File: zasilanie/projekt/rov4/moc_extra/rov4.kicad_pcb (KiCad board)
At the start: 2 copper layers, 124.5 x 68.6 mm, 18 parts, among them J43 Torpedy_serwo_7v, J44 Extra, J45 Extra, J46 Manip_serwo, J47 Extra, J48 Extra, J53 HP_IN, J60 HP_OUT, U4 lm2596, U5 lm2596

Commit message: sprzątanie
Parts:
- removed the REF** at (152.3, 101.8)
- removed the REF** at (152.3, 48.6)
- removed the REF** at (43.0, 102.0)
- removed the REF** at (43.0, 48.6)
- added REF**: MountingHole_3.2mm_M3_Pad, MountingHole:MountingHole_3.2mm_M3_Pad, F.Cu at (154.0, 29.1)
- added REF**: MountingHole_3.2mm_M3_Pad, MountingHole:MountingHole_3.2mm_M3_Pad, F.Cu at (154.0, 87.5)
- added REF**: MountingHole_3.2mm_M3_Pad, MountingHole:MountingHole_3.2mm_M3_Pad, F.Cu at (39.7, 87.5)
- added REF**: MountingHole_3.2mm_M3_Pad, MountingHole:MountingHole_3.2mm_M3_Pad, F.Cu at (39.7, 29.1)
- moved J48 111.1 mm to (47.9, 42.0), turned to 0 degrees
- moved J53 100.9 mm to (143.5, 51.1), turned to 90 degrees
- moved J44 100.6 mm to (47.9, 75.0), turned to 180 degrees
- moved J60 91.2 mm to (143.5, 69.7), turned to 90 degrees
- moved J46 89.2 mm to (60.6, 42.0), turned to 0 degrees
- moved TP8 81.2 mm to (73.3, 34.4), turned to 180 degrees
- moved J45 75.7 mm to (60.6, 75.0), turned to 180 degrees
- moved J47 69.6 mm to (73.3, 42.0), turned to 0 degrees
- moved TP7 57.8 mm to (73.3, 82.6), turned to 180 degrees
- moved J43 51.2 mm to (73.3, 75.0), turned to 180 degrees
- moved U5 49.6 mm to (107.6, 44.3), turned to 180 degrees
- moved C28 41.5 mm to (90.5, 51.0), turned to 90 degrees
- moved C27 23.6 mm to (90.5, 78.6), turned to 90 degrees
- moved U4 22.9 mm to (107.6, 72.3), turned to 180 degrees
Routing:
- net Net-(C27-Pad1): track 0.00 -> 6.37 mm
- net Net-(C28-Pad1): track 0.00 -> 6.24 mm
- added copper zone on F.Cu, net Net-(C27-Pad1)
- added copper zone on B.Cu, net Net-(C27-Pad2)
- added copper zone on F.Cu, net Net-(C28-Pad1)
- added copper zone on F.Cu, net Net-(J53-Pad1)
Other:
- rule via_min_size: 0.4 -> 0.5

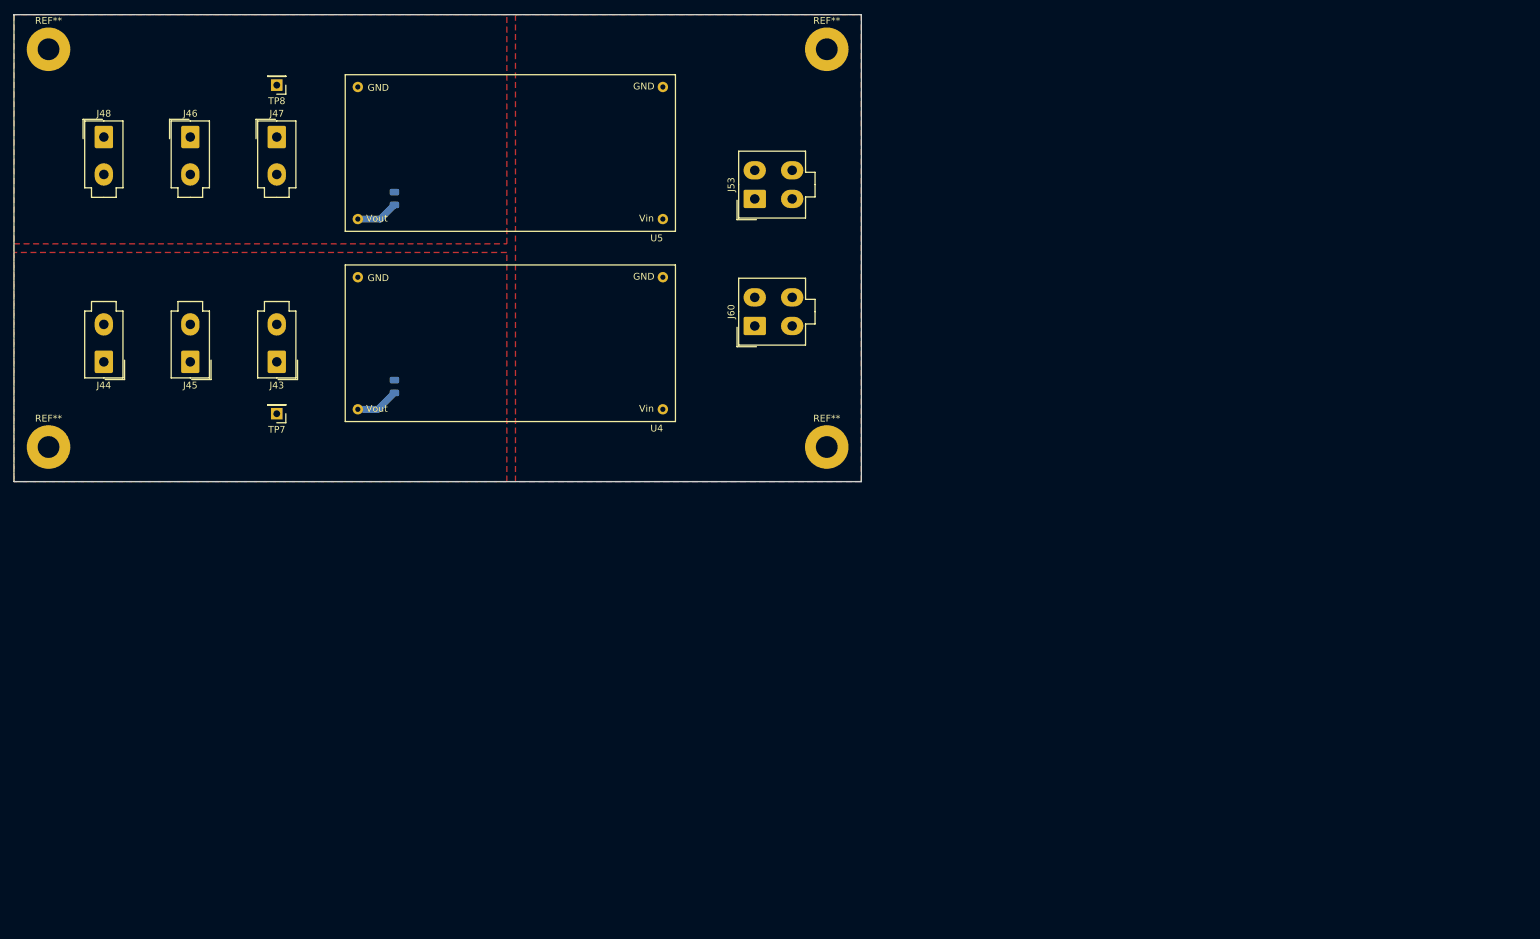
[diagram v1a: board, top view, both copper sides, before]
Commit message: battery on/off
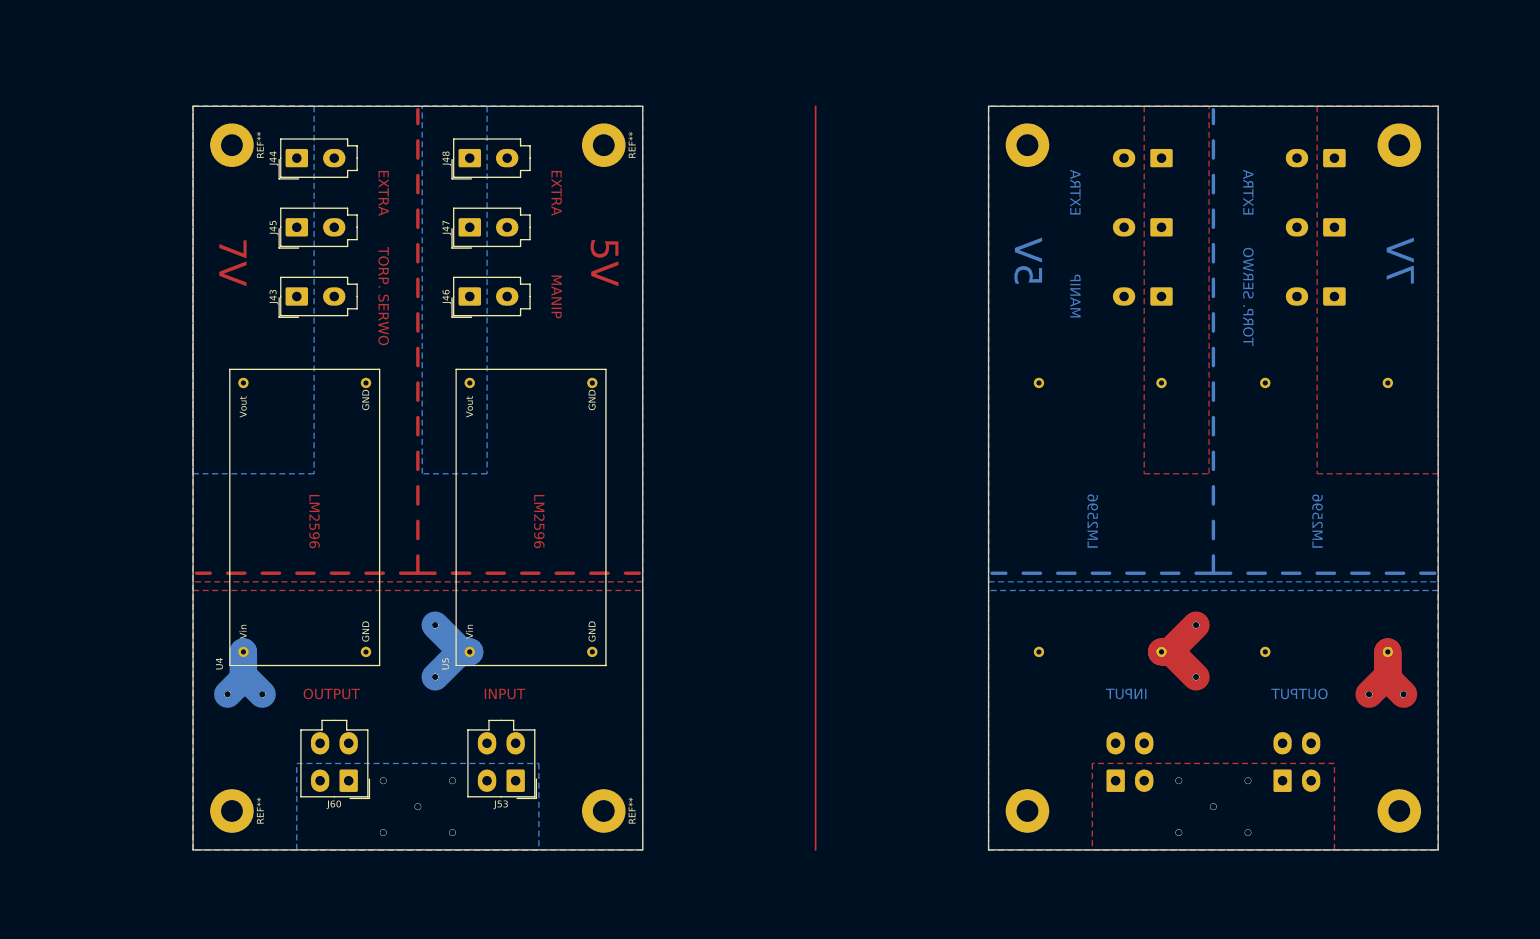
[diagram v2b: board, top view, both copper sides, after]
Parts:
- removed C27, C28: 100nF, Capacitor_SMD:C_0805_2012Metric
- removed the J43 at (73.3, 75.0)
- removed the J44 at (47.9, 75.0)
- removed the J45 at (60.6, 75.0)
- removed the J46 at (60.6, 42.0)
- removed the J47 at (73.3, 42.0)
- removed the J48 at (47.9, 42.0)
- removed the J53 at (143.5, 51.1)
- removed the J60 at (143.5, 69.7)
- removed the REF** at (154.0, 29.1)
- removed the REF** at (154.0, 87.5)
- removed the REF** at (39.7, 87.5)
- removed the REF** at (39.7, 29.1)
- removed TP7: HP_7V, Connector_PinHeader_2.54mm:PinHeader_1x01_P2.54mm_Vertical
- removed TP8: HP_5V, Connector_PinHeader_2.54mm:PinHeader_1x01_P2.54mm_Vertical
- removed the U4 at (107.6, 72.3)
- removed the U5 at (107.6, 44.3)
- added J43: Torpedy_serwo_7v, molex_3d_2pin:Molex_Mini-Fit_Jr_5566-02A_2x01_P4.20mm_Vertical, F.Cu at (76.2, 65.4)
- added J43: Torpedy_serwo_7v, molex_3d_2pin:Molex_Mini-Fit_Jr_5566-02A_2x01_P4.20mm_Vertical, B.Cu at (228.6, 65.4)
- added J44: Extra, molex_3d_2pin:Molex_Mini-Fit_Jr_5566-02A_2x01_P4.20mm_Vertical, B.Cu at (228.6, 45.1)
- added J44: Extra, molex_3d_2pin:Molex_Mini-Fit_Jr_5566-02A_2x01_P4.20mm_Vertical, F.Cu at (76.2, 45.1)
- added J45: Extra, molex_3d_2pin:Molex_Mini-Fit_Jr_5566-02A_2x01_P4.20mm_Vertical, F.Cu at (76.2, 55.2)
- added J45: Extra, molex_3d_2pin:Molex_Mini-Fit_Jr_5566-02A_2x01_P4.20mm_Vertical, B.Cu at (228.6, 55.2)
- added J46: Manip_serwo, molex_3d_2pin:Molex_Mini-Fit_Jr_5566-02A_2x01_P4.20mm_Vertical, F.Cu at (101.6, 65.4)
- added J46: Manip_serwo, molex_3d_2pin:Molex_Mini-Fit_Jr_5566-02A_2x01_P4.20mm_Vertical, B.Cu at (203.2, 65.4)
- added J47: Extra, molex_3d_2pin:Molex_Mini-Fit_Jr_5566-02A_2x01_P4.20mm_Vertical, F.Cu at (101.6, 55.2)
- added J47: Extra, molex_3d_2pin:Molex_Mini-Fit_Jr_5566-02A_2x01_P4.20mm_Vertical, B.Cu at (203.2, 55.2)
- added J48: Extra, molex_3d_2pin:Molex_Mini-Fit_Jr_5566-02A_2x01_P4.20mm_Vertical, B.Cu at (203.2, 45.1)
- added J48: Extra, molex_3d_2pin:Molex_Mini-Fit_Jr_5566-02A_2x01_P4.20mm_Vertical, F.Cu at (101.6, 45.1)
- added J53: HP_IN, Connector_Molex:Molex_Mini-Fit_Jr_5566-04A_2x02_P4.20mm_Vertical, F.Cu at (108.3, 136.5)
- added J53: HP_IN, Connector_Molex:Molex_Mini-Fit_Jr_5566-04A_2x02_P4.20mm_Vertical, B.Cu at (196.5, 136.5)
- added J60: HP_OUT, Connector_Molex:Molex_Mini-Fit_Jr_5566-04A_2x02_P4.20mm_Vertical, F.Cu at (83.8, 136.5)
- added J60: HP_OUT, Connector_Molex:Molex_Mini-Fit_Jr_5566-04A_2x02_P4.20mm_Vertical, B.Cu at (221.0, 136.5)
- added REF**: MountingHole_3.2mm_M3_Pad, MountingHole:MountingHole_3.2mm_M3_Pad, F.Cu at (121.3, 141.0)
- added REF**: MountingHole_3.2mm_M3_Pad, MountingHole:MountingHole_3.2mm_M3_Pad, F.Cu at (121.3, 43.2)
- added REF**: MountingHole_3.2mm_M3_Pad, MountingHole:MountingHole_3.2mm_M3_Pad, F.Cu at (66.7, 141.0)
- added REF**: MountingHole_3.2mm_M3_Pad, MountingHole:MountingHole_3.2mm_M3_Pad, F.Cu at (66.7, 43.2)
- added REF**: MountingHole_3.2mm_M3_Pad, MountingHole:MountingHole_3.2mm_M3_Pad, B.Cu at (238.1, 141.0)
- added REF**: MountingHole_3.2mm_M3_Pad, MountingHole:MountingHole_3.2mm_M3_Pad, B.Cu at (183.5, 141.0)
- added REF**: MountingHole_3.2mm_M3_Pad, MountingHole:MountingHole_3.2mm_M3_Pad, B.Cu at (238.1, 43.2)
- added REF**: MountingHole_3.2mm_M3_Pad, MountingHole:MountingHole_3.2mm_M3_Pad, B.Cu at (183.5, 43.2)
- added U4: lm2596, lm2596:lm2596-44_8mm_x_23mm, F.Cu at (77.4, 97.9)
- added U4: lm2596, lm2596:lm2596-44_8mm_x_23mm, B.Cu at (227.4, 97.9)
- added U5: lm2596, lm2596:lm2596-44_8mm_x_23mm, F.Cu at (110.6, 97.9)
- added U5: lm2596, lm2596:lm2596-44_8mm_x_23mm, B.Cu at (194.2, 97.9)
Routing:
- net (no net): track 0.00 -> 178.8 mm
- net Net-(C27-Pad2): track 0.00 -> 69.6 mm
- net Net-(J53-Pad1): track 0.00 -> 55.7 mm, vias 0 -> 18
- net Net-(C27-Pad1): track 6.37 -> 0.00 mm
- net Net-(C28-Pad1): track 6.24 -> 0.00 mm
- added copper zone on B.Cu, net Net-(C27-Pad1)
- added copper zone on F.Cu, net Net-(C27-Pad2)
- added copper zone on B.Cu, net Net-(C28-Pad1)
- added copper zone on B.Cu, net Net-(J53-Pad1)
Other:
- board size 124.5 x 68.6 mm -> 182.9 x 109.2 mm
- board text added: "5V"
- board text added: "7V"
- board text added: "EXTRA"
- board text added: "INPUT"
- board text added: "LM2596"
- board text added: "MANIP"
- board text added: "OUTPUT"
- board text added: "TORP. SERWO"

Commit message: poprawki/schematy
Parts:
- removed the J43 at (228.6, 65.4)
- removed the J44 at (228.6, 45.1)
- removed the J44 at (76.2, 45.1)
- removed the J45 at (228.6, 55.2)
- removed the J46 at (203.2, 65.4)
- removed the J47 at (203.2, 55.2)
- removed the J48 at (203.2, 45.1)
- removed the J53 at (196.5, 136.5)
- removed the J60 at (221.0, 136.5)
- removed the REF** at (238.1, 141.0)
- removed the REF** at (183.5, 141.0)
- removed the REF** at (238.1, 43.2)
- removed the REF** at (183.5, 43.2)
- removed the U4 at (227.4, 97.9)
- removed the U5 at (194.2, 97.9)
- added J44: Extra, molex_3d_2pin:Molex_Mini-Fit_Jr_5566-02A_2x01_P4.20mm_Vertical, F.Cu at (114.9, 108.0)
- REF** (x2): value MountingHole_3.2mm_M3_Pad -> mnt
- moved REF** 146.0 mm to (210.8, 117.5), turned to 0 degrees
- moved J60 127.8 mm to (206.4, 100.3), turned to 270 degrees
- moved REF** 118.8 mm to (210.8, 62.9), turned to 0 degrees
- moved J53 115.3 mm to (206.4, 75.8), turned to 270 degrees
- moved U4 90.8 mm to (167.7, 106.8), turned to 180 degrees
- moved REF** 87.6 mm to (113.0, 117.5), turned to 0 degrees
- moved J43 72.8 mm to (135.3, 108.0), turned to 180 degrees
- moved J45 71.9 mm to (125.1, 108.0), turned to 180 degrees
- moved U5 62.1 mm to (167.7, 73.5), turned to 180 degrees
- moved J48 39.8 mm to (114.9, 82.5), turned to 180 degrees
- moved J46 37.8 mm to (135.3, 82.5), turned to 180 degrees
- moved J47 36.0 mm to (125.1, 82.5), turned to 180 degrees
- moved REF** 21.3 mm to (113.0, 62.9), turned to 0 degrees
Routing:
- net (no net): track 178.8 -> 1326.9 mm
- net Net-(C27-Pad2): track 69.6 -> 0.00 mm
- net Net-(J53-Pad1): track 55.7 -> 27.9 mm, vias 18 -> 7
- removed copper zone on F.Cu, net Net-(C27-Pad1)
- removed copper zone on F.Cu, net Net-(C28-Pad1)
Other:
- board size 182.9 x 109.2 mm -> 109.2 x 66 mm
